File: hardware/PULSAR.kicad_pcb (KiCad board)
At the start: 4 copper layers, 9 parts, among them J1 Conn_01x20, J2 Conn_01x04, J3 USB_C_Receptacle, U1 AP2112K-3.3, U2 SS49E, U3 CD74HC4067M, U4 ADS8688

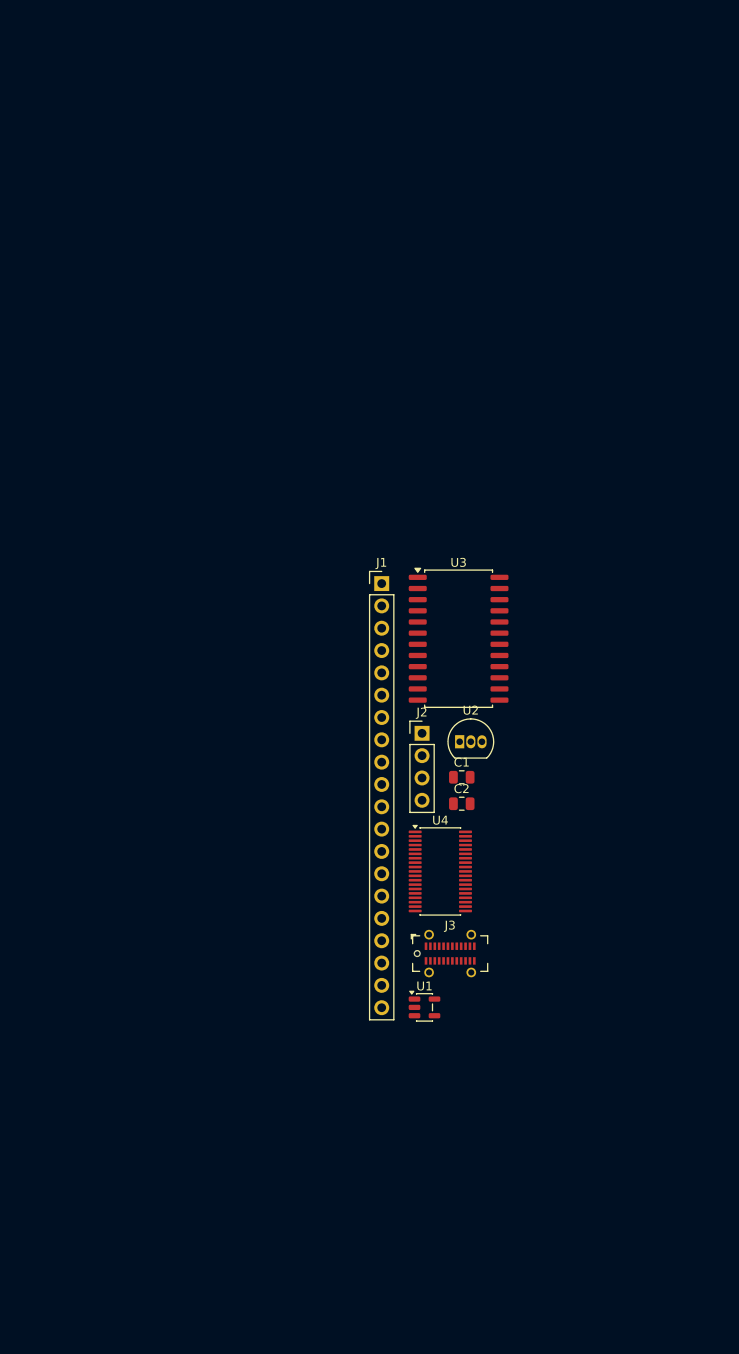
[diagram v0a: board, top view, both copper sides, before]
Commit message: feat: initial PCB layout component placement
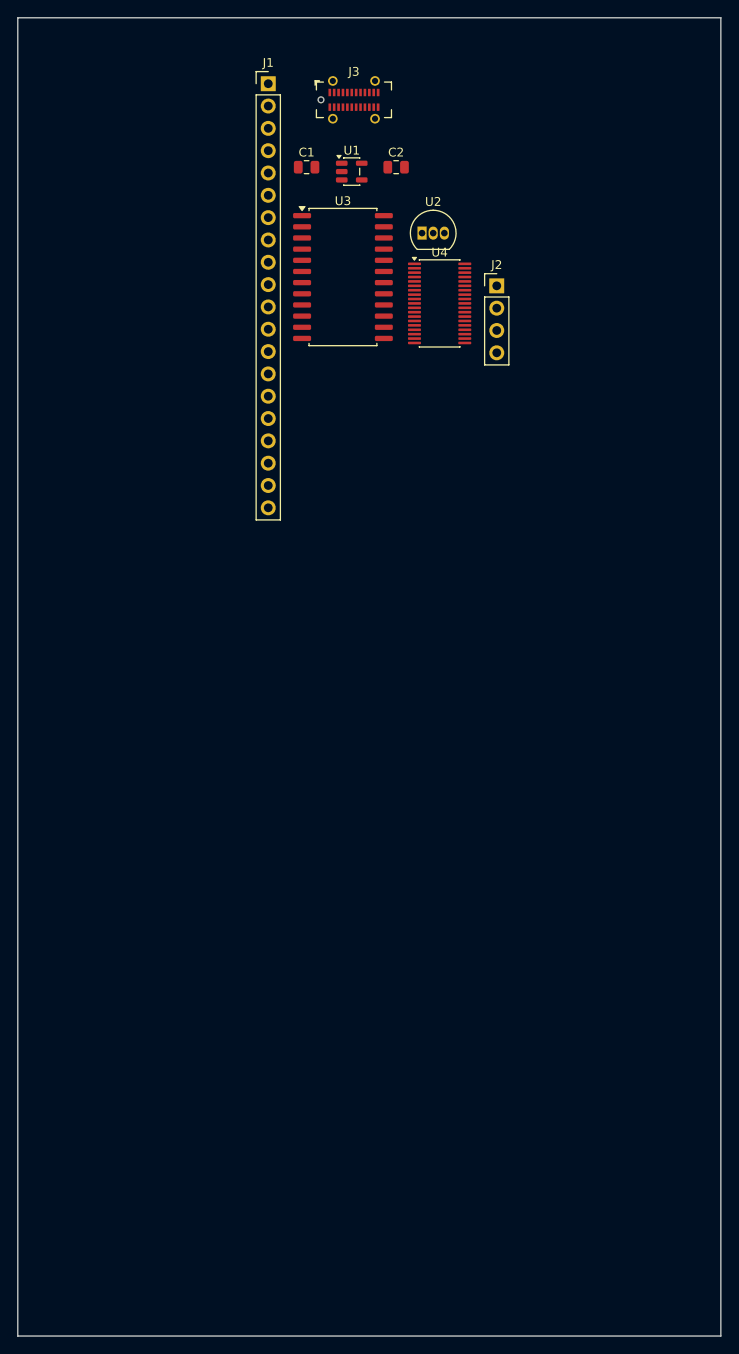
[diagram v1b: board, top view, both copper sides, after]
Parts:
- moved J3 97.8 mm to (141.8, 23.3)
- moved U1 95.5 mm to (141.5, 31.5)
- moved C2 72.8 mm to (146.6, 31.0)
- moved C1 71.6 mm to (136.4, 31.0)
- moved U4 64.6 mm to (151.5, 46.5)
- moved J1 58.3 mm to (132.0, 21.5)
- moved U2 58.0 mm to (149.5, 38.5)
- moved J2 51.6 mm to (158.0, 44.5)
- moved U3 43.2 mm to (140.5, 43.5)
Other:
- board outline added: 80 x 150 mm
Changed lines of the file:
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@@
 	(footprint "Package_TO_SOT_THT:TO-92_Inline"
 		(layer "F.Cu")
-		(at 153.78 96.38)
+		(at 149.5 38.5)
 		(descr "TO-92 leads in-line, narrow, oval pads, drill 0.75mm (see NXP sot054_po.pdf)")
 		(tags "to-92 sc-43 sc-43a sot54 PA33 transistor")
@@
 	(footprint "Capacitor_SMD:C_0805_2012Metric"
 		(layer "F.Cu")
-		(at 154.02 100.42)
+		(at 136.3625 31)
 		(descr "Capacitor SMD 0805 (2012 Metric), square (rectangular) end terminal, IPC-7351 nominal, (Body size source: IPC-SM-782 page 76, https://www.pcb-3d.com/wordpress/wp-content/uploads/ipc-sm-782a_amendment_1_and_2.pdf, https://docs.google.com/spreadsheets/d/1BsfQQcO9C6DZCsRaXUlFlo91Tg2WpOkGARC1WS5S8t0/edit?usp=sharing)")
 		(tags "capacitor")
@@
 	(footprint "Package_SO:SOIC-24W_7.5x15.4mm_P1.27mm"
 		(layer "F.Cu")
-		(at 153.66 84.655)
+		(at 140.5 43.5)
 		(descr "SOIC, 24 Pin (JEDEC MS-013AD, https://www.analog.com/media/en/package-pcb-resources/package/pkg_pdf/soic_wide-rw/RW_24.pdf)")
 		(tags "SOIC SO")
@@
 	(footprint "Connector_USB:USB_C_Receptacle_GCT_USB4115-03-C"
 		(layer "F.Cu")
-		(at 152.7 120.48)
+		(at 141.75 23.335)
 		(descr "USB TYPE C, VERT RCPT PCB, SMT, https://gct.co/files/drawings/usb4115.pdf")
 		(tags "USB C Type-C Receptacle SMD")
@@
 			(polygon
 				(pts
-					(xy 153.5 118.68) (xy 151.9 118.68) (xy 151.9 117.98) (xy 153.5 117.98)
+					(xy 142.55 21.535) (xy 140.95 21.535) (xy 140.95 20.835) (xy 142.55 20.835)
 				)
 			)
@@
 			(polygon
 				(pts
-					(xy 153.5 122.98) (xy 151.9 122.98) (xy 151.9 122.28) (xy 153.5 122.28)
+					(xy 142.55 25.835) (xy 140.95 25.835) (xy 140.95 25.135) (xy 142.55 25.135)
 				)
 			)
@@
 	(footprint "Package_TO_SOT_SMD:SOT-23-5"
 		(layer "F.Cu")
-		(at 149.78 126.605)
+		(at 141.5 31.5)
 		(descr "SOT, 5 Pin (JEDEC MO-178 Var AA https://www.jedec.org/document_search?search_api_views_fulltext=MO-178)")
 		(tags "SOT TO_SOT_SMD")
@@
 	(footprint "Connector_PinHeader_2.54mm:PinHeader_1x04_P2.54mm_Vertical"
 		(layer "F.Cu")
-		(at 149.5 95.42)
+		(at 158 44.5)
 		(descr "Through hole straight pin header, 1x04, 2.54mm pitch, single row")
 		(tags "Through hole pin header THT 1x04 2.54mm single row")
@@
 	(footprint "Package_SO:TSSOP-38_4.4x9.7mm_P0.5mm"
 		(layer "F.Cu")
-		(at 151.58 111.135)
+		(at 151.5 46.5)
 		(descr "TSSOP, 38 Pin (JEDEC MO-153 Var BD https://www.jedec.org/document_search?search_api_views_fulltext=MO-153)")
 		(tags "TSSOP SO")
@@
 	(footprint "Connector_PinHeader_2.54mm:PinHeader_1x20_P2.54mm_Vertical"
 		(layer "F.Cu")
-		(at 144.91 78.38)
+		(at 132 21.5)
 		(descr "Through hole straight pin header, 1x20, 2.54mm pitch, single row")
 		(tags "Through hole pin header THT 1x20 2.54mm single row")
@@
 	(footprint "Capacitor_SMD:C_0805_2012Metric"
 		(layer "F.Cu")
-		(at 154.02 103.43)
+		(at 146.55 31)
 		(descr "Capacitor SMD 0805 (2012 Metric), square (rectangular) end terminal, IPC-7351 nominal, (Body size source: IPC-SM-782 page 76, https://www.pcb-3d.com/wordpress/wp-content/uploads/ipc-sm-782a_amendment_1_and_2.pdf, https://docs.google.com/spreadsheets/d/1BsfQQcO9C6DZCsRaXUlFlo91Tg2WpOkGARC1WS5S8t0/edit?usp=sharing)")
 		(tags "capacitor")
@@
 		)
 	)
+	(gr_rect
+		(start 103.5 14)
+		(end 183.5 164)
+		(stroke
+			(width 0.05)
+			(type default)
+		)
+		(fill no)
+		(layer "Edge.Cuts")
+	)
 	(embedded_fonts no)
